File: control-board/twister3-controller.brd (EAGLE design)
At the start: 191 x 90.5 mm, 58 parts, among them J1 BARREL-JACK_PJ-063BH, J5 OSTVN04A150, U1 IS31FL3193, U2 MIC4680-5.0YM-TR, U3 MAX6816, U4 TMC2130-LA, U5 Teensy 3.2, U6 GDM1602K

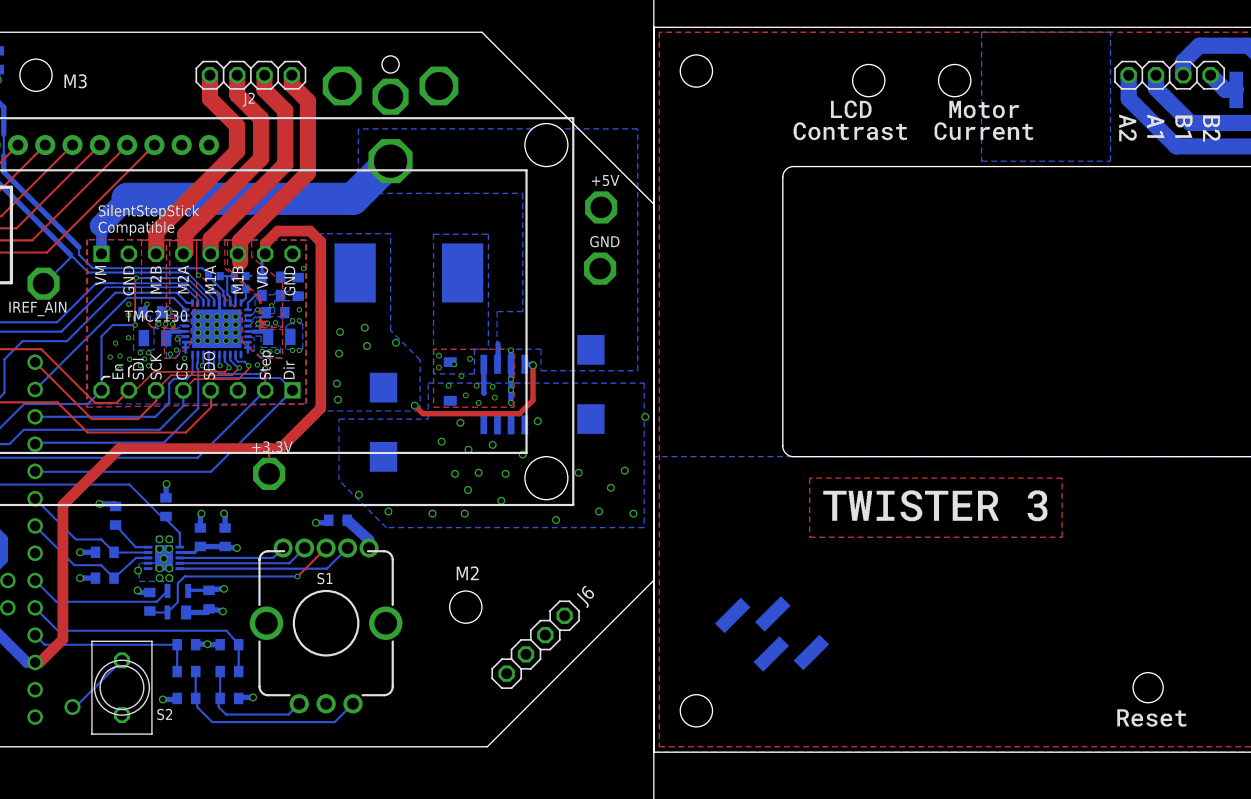
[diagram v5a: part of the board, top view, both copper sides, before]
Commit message: Removed trimpot access in control board front panel
- Trimpots should be set during assembly and glued, access is not
required during operaiton. Also, current trimpot only works if the
silent stepper stick module is not used with is not the default case.
- Also, removed reset switch (since this can be done by removing
power...)
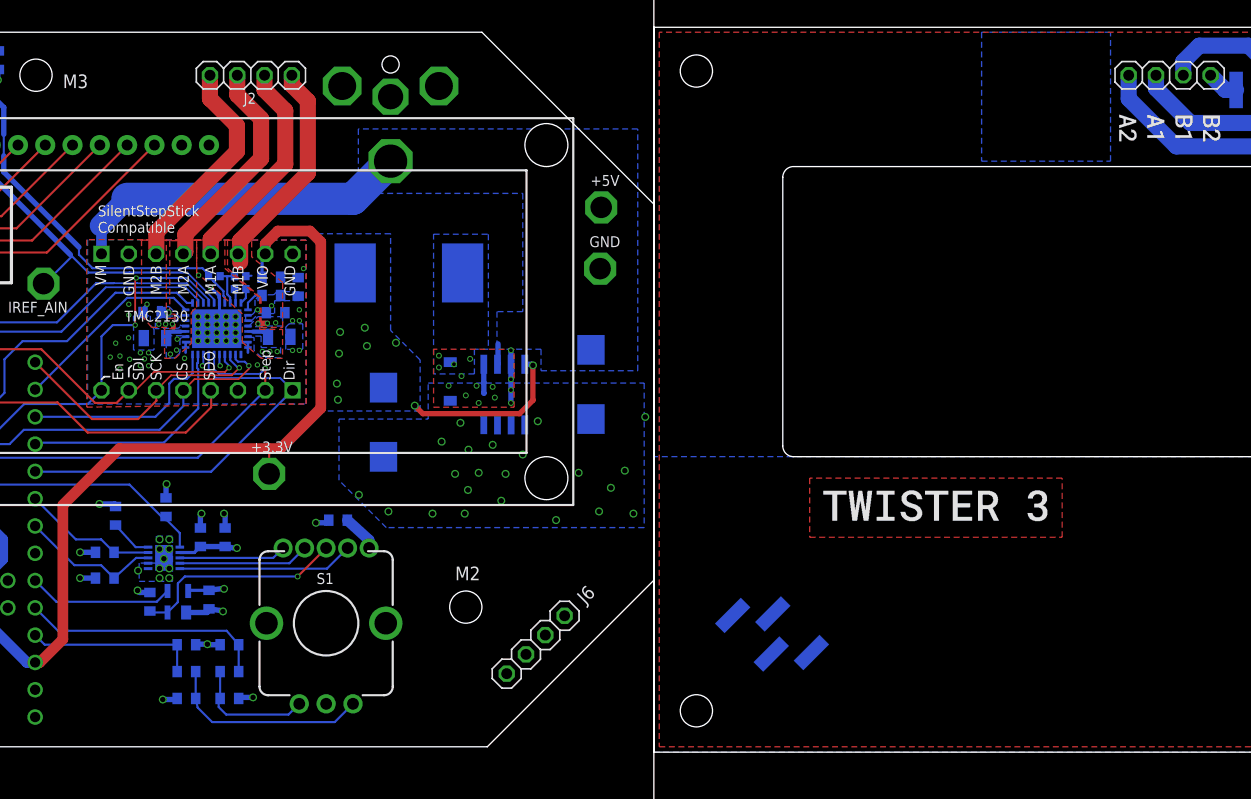
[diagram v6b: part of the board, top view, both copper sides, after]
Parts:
- removed S2: 800AWSP9M2QE, jonnew:800AWSP9M2QE
- removed TP1: RESET, jonnew:TESTPOINT_1MM
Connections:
- removed net N$23: S2.1, TP1.1
- net GND: no longer S2.2
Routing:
- net N$23: track 6.40 -> 0.00 mm
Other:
- outline, holes or cut-outs redrawn
